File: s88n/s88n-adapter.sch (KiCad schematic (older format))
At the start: 4 parts, among them J1 RJ45, P1 S88, P2 PWR, P3 Power

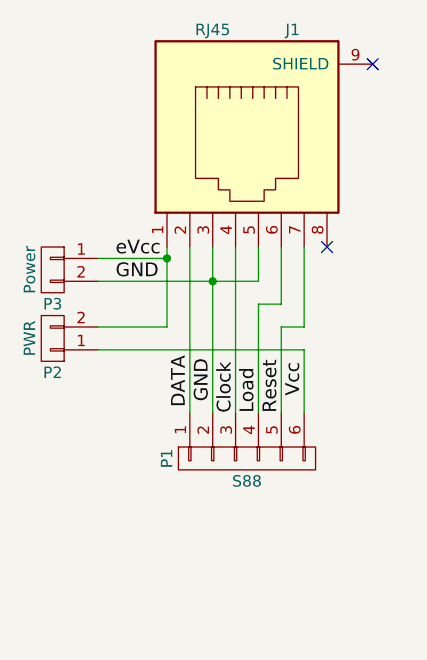
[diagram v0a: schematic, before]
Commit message: add template
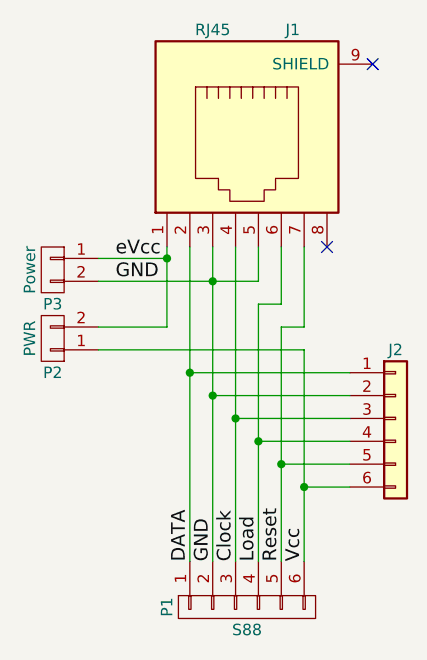
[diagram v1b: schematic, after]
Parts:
- added J2: Conn_01x06, Pin_Headers:Pin_Header_Straight_1x06_Pitch2.54mm, symbol Conn_01x06
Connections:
- net Clock: now also J2.3 (Pin_3)
- net DATA: now also J2.1 (Pin_1)
- net GND: now also J2.2 (Pin_2)
- net Load: now also J2.4 (Pin_4)
- net Reset: now also J2.5 (Pin_5)
- net Vcc: now also J2.6 (Pin_6)
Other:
- moved on the sheet: P1
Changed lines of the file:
@@
 $EndComp
 Wire Wire Line
-	4200 4300 4200 5025
+	4200 4300 4200 5675
 $Comp
 L CONN_01X02 P3
@@
 	-1   0    0    -1
 $EndComp
-Text Label 4200 5000 1    60   ~ 0
+Text Label 4200 5675 1    60   ~ 0
 DATA
 $Comp
@@
 eVcc
 Wire Wire Line
-	4300 4300 4300 5025
+	4300 4300 4300 5675
 Wire Wire Line
 	3800 4450 4500 4450
 Connection ~ 4300 4450
 Wire Wire Line
-	4400 4300 4400 5025
+	4400 4300 4400 5675
 Text Label 3875 4450 0    60   ~ 0
 GND
@@
 L CONN_01X06 P1
 U 1 1 5B644280
-P 4450 5225
-F 0 "P1" H 4450 5575 50  0000 C CNN
-F 1 "S88" V 4550 5225 50  0000 C CNN
-F 2 "Pin_Headers:Pin_Header_Angled_1x06" H 4450 5225 50  0001 C CNN
-F 3 "" H 4450 5225 50  0000 C CNN
-	1    4450 5225
+P 4450 5875
+F 0 "P1" H 4450 6225 50  0000 C CNN
+F 1 "S88" V 4550 5875 50  0000 C CNN
+F 2 "Pin_Headers:Pin_Header_Angled_1x06" H 4450 5875 50  0001 C CNN
+F 3 "" H 4450 5875 50  0000 C CNN
+	1    4450 5875
 	0    -1   1    0
 $EndComp
@@
 	4600 4550 4500 4550
 Wire Wire Line
-	4500 4550 4500 5025
+	4500 4550 4500 5675
 Wire Wire Line
 	4700 4300 4700 4650
@@
 	4700 4650 4600 4650
 Wire Wire Line
-	4600 4650 4600 5025
+	4600 4650 4600 5675
 Wire Wire Line
 	4100 4650 3800 4650
@@
 	3800 4750 4700 4750
 Wire Wire Line
-	4700 4750 4700 5025
-Text Label 4400 5025 1    60   ~ 0
+	4700 4750 4700 5675
+Text Label 4400 5675 1    60   ~ 0
 Clock
-Text Label 4500 5025 1    60   ~ 0
+Text Label 4500 5675 1    60   ~ 0
 Load
-Text Label 4600 5025 1    60   ~ 0
+Text Label 4600 5675 1    60   ~ 0
 Reset
 NoConn ~ 4800 4300
 NoConn ~ 5000 3500
-Text Label 4300 4975 1    60   ~ 0
+Text Label 4300 5675 1    60   ~ 0
 GND
-Text Label 4700 4950 1    60   ~ 0
+Text Label 4700 5675 1    60   ~ 0
 Vcc
+$Comp
+L Conn_01x06 J2
+U 1 1 5B649124
+P 5100 5050
+F 0 "J2" H 5100 5350 50  0000 C CNN
+F 1 "Conn_01x06" V 5100 4650 50  0001 C CNN
+F 2 "Pin_Headers:Pin_Header_Straight_1x06_Pitch2.54mm" H 5100 5050 50  0001 C CNN
+F 3 "" H 5100 5050 50  0001 C CNN
+	1    5100 5050
+	1    0    0    -1
+$EndComp
+Wire Wire Line
+	4200 4850 4900 4850
+Connection ~ 4200 4850
+Wire Wire Line
+	4900 4950 4300 4950
+Connection ~ 4300 4950
+Wire Wire Line
+	4900 5050 4400 5050
+Connection ~ 4400 5050
+Wire Wire Line
+	4900 5150 4500 5150
+Connection ~ 4500 5150
+Wire Wire Line
+	4900 5250 4600 5250
+Connection ~ 4600 5250
+Wire Wire Line
+	4900 5350 4700 5350
+Connection ~ 4700 5350
 $EndSCHEMATC
